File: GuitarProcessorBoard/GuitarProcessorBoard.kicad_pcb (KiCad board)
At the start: 4 copper layers, 86 x 65 mm, 136 parts, among them J301 SWD Header, J302 PWR, J303 TAP, J304 MODE, J305 BYP, J306 EXP, J307 ScopeGroundLoop, SW301 RST, SW302 BOOT, U201 TLV320AIC3204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

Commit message: enclosure SVG stuff
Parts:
- U303: value SSD1306_OLED_128x64 -> ~

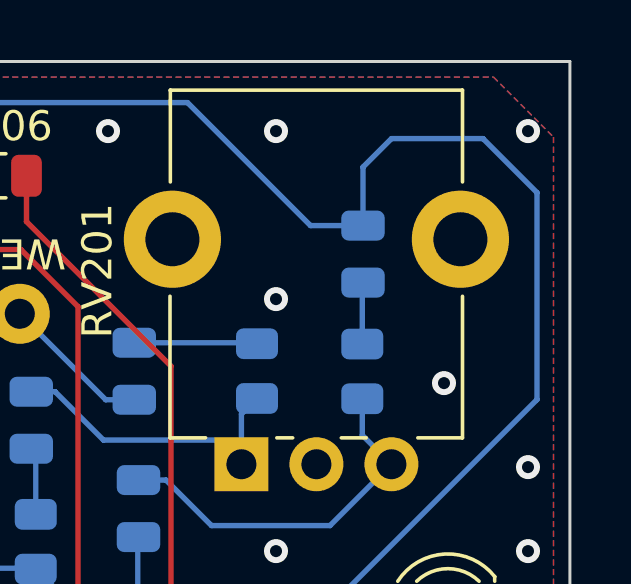
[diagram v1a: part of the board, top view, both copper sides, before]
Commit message: processing callback set up
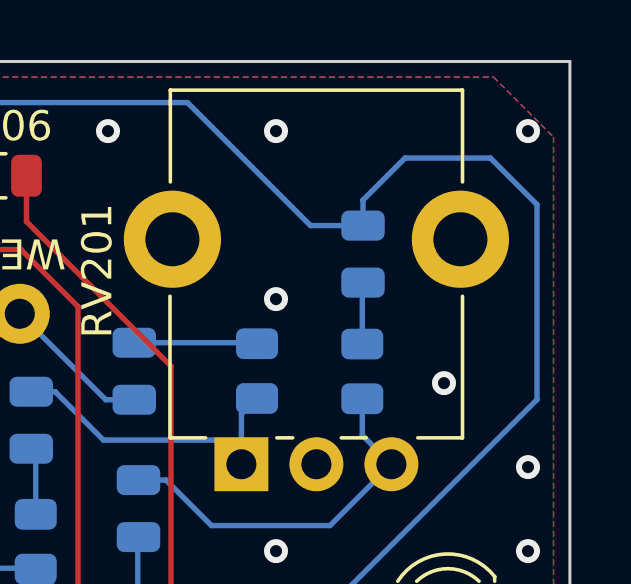
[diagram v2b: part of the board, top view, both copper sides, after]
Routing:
- net FX_IN: track 134.8 -> 133.4 mm
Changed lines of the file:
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@@
 	)
 	(footprint "Potentiometer_THT:Potentiometer_Alpha_RD901F-40-00D_Single_Vertical_CircularHoles"
+		(locked yes)
 		(layer "F.Cu")
 		(at -165.4 86.249999 90)
@@
 	)
 	(footprint "Potentiometer_THT:Potentiometer_Alpha_RD901F-40-00D_Single_Vertical_CircularHoles"
+		(locked yes)
 		(layer "F.Cu")
 		(at -103.903222 44.405189 90)
@@
 	)
 	(footprint "Potentiometer_THT:Potentiometer_Alpha_RD901F-40-00D_Single_Vertical_CircularHoles"
+		(locked yes)
 		(layer "F.Cu")
 		(at -140.348389 86.199999 90)
@@
 	)
 	(footprint "Potentiometer_THT:Potentiometer_Alpha_RD901F-40-00D_Single_Vertical_CircularHoles"
+		(locked yes)
 		(layer "F.Cu")
 		(at -115.296778 86.31981 90)
@@
 	)
 	(segment
-		(start -102.2 50.4)
-		(end -94.05 42.25)
+		(start -132.9 91.15)
+		(end -129.55 87.8)
 		(width 0.18)
 		(layer "B.Cu")
@@
 	)
 	(segment
-		(start -94.05 42.25)
-		(end -94.05 35.35)
+		(start -121.7 32.35)
+		(end -128.500001 39.150001)
 		(width 0.18)
 		(layer "B.Cu")
@@
 	)
 	(segment
-		(start -99.85 34.5)
-		(end -99.85 36.450001)
+		(start -98.45 34.2)
+		(end -99.85 35.6)
 		(width 0.18)
 		(layer "B.Cu")
@@
 	)
 	(segment
-		(start -132.9 91.15)
-		(end -129.55 87.8)
+		(start -102.2 50.4)
+		(end -94.05 42.25)
 		(width 0.18)
 		(layer "B.Cu")
@@
 	)
 	(segment
-		(start -121.7 32.35)
-		(end -128.500001 39.150001)
+		(start -132.9 92.8)
+		(end -132.9 91.15)
 		(width 0.18)
 		(layer "B.Cu")
@@
 	)
 	(segment
-		(start -94.05 35.35)
-		(end -95.85 33.55)
+		(start -101.599999 36.450001)
+		(end -105.7 32.35)
 		(width 0.18)
 		(layer "B.Cu")
@@
 	)
 	(segment
-		(start -95.85 33.55)
-		(end -98.9 33.55)
+		(start -94.05 42.25)
+		(end -94.05 35.75)
 		(width 0.18)
 		(layer "B.Cu")
@@
 	)
 	(segment
-		(start -132.9 92.8)
-		(end -132.9 91.15)
+		(start -99.85 35.6)
+		(end -99.85 36.450001)
 		(width 0.18)
 		(layer "B.Cu")
@@
 	)
 	(segment
-		(start -101.599999 36.450001)
-		(end -105.7 32.35)
+		(start -129.55 87.8)
+		(end -129.55 85.75)
 		(width 0.18)
 		(layer "B.Cu")
@@
 	)
 	(segment
-		(start -129.55 87.8)
-		(end -129.55 85.75)
+		(start -95.6 34.2)
+		(end -98.45 34.2)
 		(width 0.18)
 		(layer "B.Cu")
@@
 	)
 	(segment
-		(start -128.500001 39.150001)
-		(end -128.500001 45.7)
+		(start -94.05 35.75)
+		(end -95.6 34.2)
 		(width 0.18)
 		(layer "B.Cu")
@@
 	)
 	(segment
-		(start -98.9 33.55)
-		(end -99.85 34.5)
+		(start -128.500001 39.150001)
+		(end -128.500001 45.7)
 		(width 0.18)
 		(layer "B.Cu")

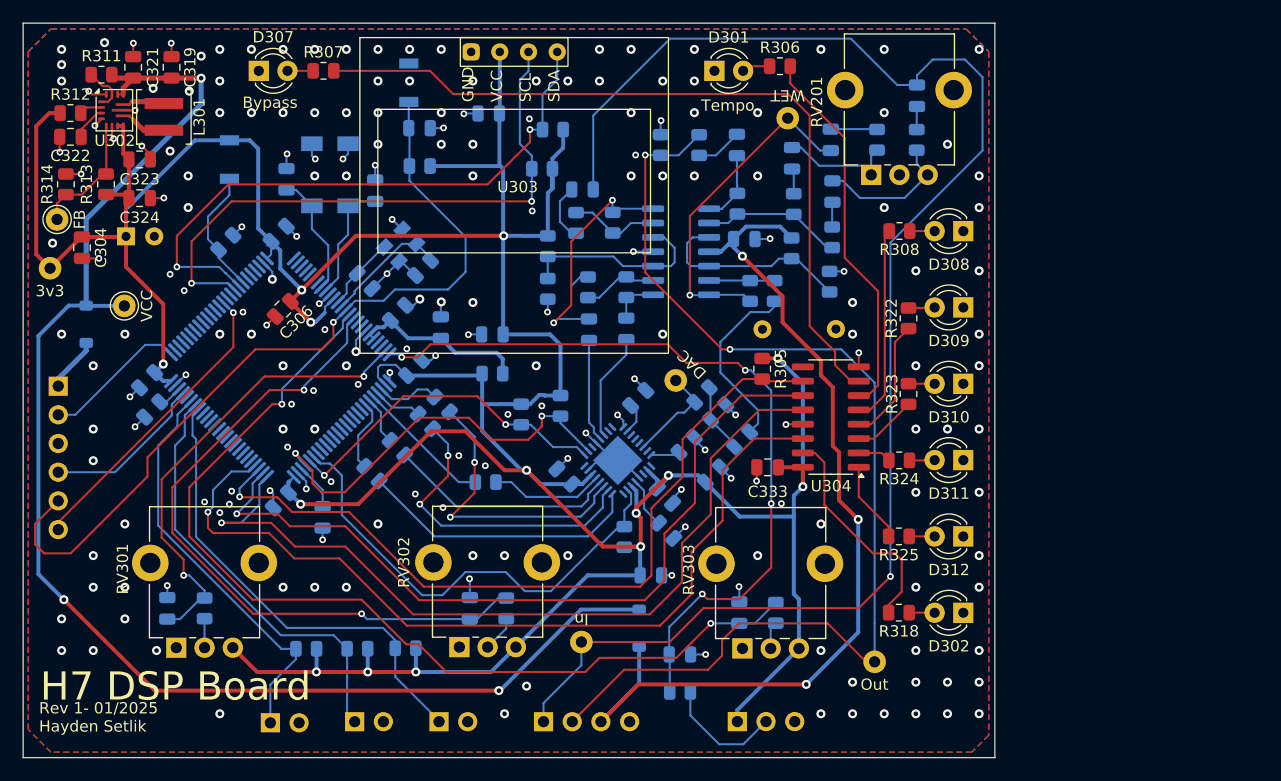
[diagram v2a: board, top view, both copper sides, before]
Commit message: differential output sim
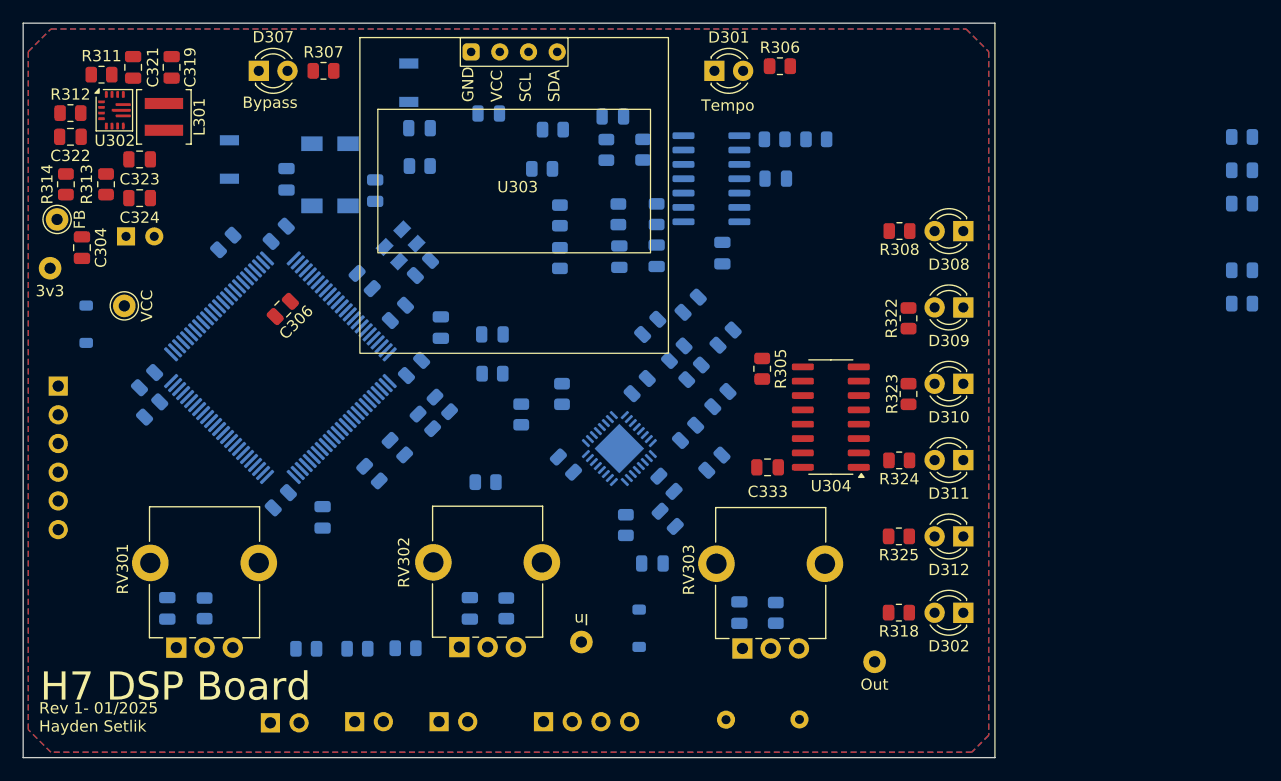
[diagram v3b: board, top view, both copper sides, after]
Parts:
- removed C217, C218: 100n, Capacitor_SMD:C_0805_2012Metric
- removed C219: 1u, Capacitor_SMD:C_0805_2012Metric
- removed C334: 10n, Capacitor_SMD:C_0805_2012Metric
- removed J306: EXP, Connector_PinHeader_2.54mm:PinHeader_1x03_P2.54mm_Vertical
- removed R217: 1M, Resistor_SMD:R_0805_2012Metric
- removed R218, R219: 10k, Resistor_SMD:R_0805_2012Metric
- removed R329: 470k, Resistor_SMD:R_0805_2012Metric
- removed RV201: 100kB, Potentiometer_THT:Potentiometer_Alpha_RD901F-40-00D_Single_Vertical_CircularHoles
- removed TP202: DAC, TestPoint:TestPoint_THTPad_D2.0mm_Drill1.0mm_VAL
- removed TP203: WET, TestPoint:TestPoint_THTPad_D2.0mm_Drill1.0mm_VAL
- added C208: 100n, Capacitor_SMD:C_0805_2012Metric, B.Cu at (-116.8, 58.8)
- C207: value 1u -> 4n7
- C214: value 1u -> 100n
- R204: value 470k -> 51k
- R205: value 470k -> 100k
- R213: value 47k -> 470k
- R214: value 47k -> 1k
- U303: value ~ -> SSD1306_OLED_128x64
- moved R212 44.8 mm to (-71.1, 44.0), turned to 180 degrees
- moved R211 43.6 mm to (-71.1, 41.0), turned to 180 degrees
- moved R215 40.1 mm to (-71.1, 52.9), turned to 180 degrees
- moved R216 36.7 mm to (-71.1, 55.8), turned to 180 degrees
- moved J307 34.7 mm to (-113.7, 92.6)
- moved R213 32.8 mm to (-71.1, 47.0), turned to 180 degrees
- moved C207 32.0 mm to (-117.2, 64.2), turned to 45 degrees
- moved R214 28.5 mm to (-119.6, 61.9), turned to 45 degrees
- moved C215 13.9 mm to (-117.1, 51.3), turned to -90 degrees
- moved C214 12.8 mm to (-119.9, 55.9)
- moved R210 12.7 mm to (-108.8, 41.3), turned to 0 degrees
- moved R209 9.76 mm to (-112.4, 41.3), turned to 0 degrees
- moved C212 9.66 mm to (-123.5, 57.9), turned to -135 degrees
- moved R205 7.00 mm to (-124.1, 42.2)
- moved C209 7.00 mm to (-126.8, 39.2)
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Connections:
- net /Audio/DAC_OUT renamed Net-(U201-OUT_L)
- C201 pad 1: +3.3V -> +3.3VA
- C202 pad 1: +3.3V -> +3.3VA
- C203 pad 1: +3.3V -> +3.3VA
- C207 pad 1: FX_IN -> Net-(C207-Pad1)
- C207 pad 2: Net-(C207-Pad2) -> GND
- C215 pad 2: Net-(C215-Pad2) -> FX_OUT
- R201 pad 1: +3.3V -> +3.3VA
- R202 pad 1: +3.3V -> +3.3VA
- R209 pad 2: /Audio/Bias2 -> Net-(U202A-+)
- R210 pad 1: /Audio/Bias2 -> Net-(U202A-+)
- R213 pad 1: Net-(C215-Pad2) -> /Audio/Bias2
- R213 pad 2: Net-(C217-Pad1) -> Net-(U202B--)
- R214 pad 1: Net-(C207-Pad2) -> Net-(U201-OUT_R)
- R214 pad 2: Net-(C218-Pad1) -> Net-(C207-Pad1)
- R215 pad 2: Net-(U202A--) -> Net-(U202B-+)
- R216 pad 1: Net-(C218-Pad2) -> Net-(U202B-+)
- R216 pad 2: Net-(U202A--) -> /Audio/Bias2
- U201 pad 23: unconnected-(U201-OUT_R-Pad23) -> Net-(U201-OUT_R)
- U201 pad 26: +3.3V -> +3.3VA
- U201 pad 30: +3.3V -> +3.3VA
- U201 pad 6: +3.3V -> +3.3VA
- U202 pad 1: Net-(C219-Pad1) -> /Audio/Bias2
- U202 pad 2: Net-(U202A--) -> /Audio/Bias2
- U202 pad 3: /Audio/Bias2 -> Net-(U202A-+)
- U202 pad 5: /Audio/Bias2 -> Net-(U202B-+)
- U301 pad 25: ADC_EXP -> unconnected-(U301-PA3-Pad25)
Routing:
- net +3.3V: track 363.5 -> 0.00 mm, vias 14 -> 0
- net FX_IN: track 133.4 -> 0.00 mm, vias 1 -> 0
- net VCC: track 124.9 -> 0.00 mm, vias 3 -> 0
- net FX_OUT: track 97.5 -> 0.00 mm, vias 2 -> 0
- net GND: track 85.7 -> 0.00 mm, vias 204 -> 0
- net ADC_C: track 85.4 -> 0.00 mm, vias 2 -> 0
- net +9V: track 82.1 -> 0.00 mm, vias 3 -> 0
- net LED_DATA: track 76.1 -> 0.00 mm, vias 1 -> 0
- net LED_LATCH: track 74.0 -> 0.00 mm, vias 1 -> 0
- net NRST: track 72.3 -> 0.00 mm, vias 1 -> 0
- net LED_SCK: track 70.9 -> 0.00 mm, vias 1 -> 0
- net /MCU/LED_BYPASS: track 69.5 -> 0.00 mm
- net LED_NRST: track 69.2 -> 0.00 mm, vias 1 -> 0
- net ADC_EXP: track 69.0 -> 0.00 mm, vias 4 -> 0
- net ADC_B: track 60.9 -> 0.00 mm, vias 2 -> 0
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
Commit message: routing start
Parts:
- removed D303: PMEG3030, Diode_SMD:D_SOD-123
- removed J303: TAP, Connector_PinHeader_2.54mm:PinHeader_1x02_P2.54mm_Vertical
- removed R213: 470k, Resistor_SMD:R_0805_2012Metric
- removed R326: 100k, Resistor_SMD:R_0805_2012Metric
- removed TP304: VCC, TestPoint:TestPoint_THTPad_D2.0mm_Drill1.0mm_VAL
- C215: value 1u -> 100n
- R211, R215: value 470k -> 100k
- R212, R216: value 470k -> 51k
- moved R212 41.1 mm to (-111.9, 48.5), turned to -90 degrees
- moved R211 38.4 mm to (-108.7, 48.6), turned to 90 degrees
- moved R216 36.3 mm to (-105.7, 45.0), turned to 90 degrees
- moved R215 34.9 mm to (-105.7, 48.6), turned to 90 degrees
- moved C303 30.8 mm to (-154.1, 77.6)
- moved J304 8.03 mm to (-157.6, 93.0)
- moved J305 6.37 mm to (-148.5, 93.2)
- moved R220 3.22 mm to (-134.8, 72.1)
- moved FB301 1.07 mm to (-137.4, 60.9), turned to 0 degrees
- moved C201 0.67 mm to (-121.5, 72.1)
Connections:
- J301 pad 1: Net-(D303-A) -> +3.3V
- U301 pad 70: TAP_BTN -> unconnected-(U301-PA11-Pad70)
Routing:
- net +3.3V: track 0.00 -> 140.8 mm, vias 0 -> 6
- net VCC: track 0.00 -> 137.3 mm, vias 0 -> 3
- net ADC_C: track 0.00 -> 106.9 mm, vias 0 -> 2
- net GND: track 0.00 -> 82.8 mm, vias 0 -> 51
- net LED_DATA: track 0.00 -> 80.3 mm, vias 0 -> 1
- net ADC_B: track 0.00 -> 79.5 mm, vias 0 -> 2
- net LED_LATCH: track 0.00 -> 75.8 mm, vias 0 -> 1
- net /MCU/LED_BYPASS: track 0.00 -> 69.0 mm
- net LED_NRST: track 0.00 -> 68.1 mm, vias 0 -> 1
- net LED_SCK: track 0.00 -> 67.2 mm, vias 0 -> 1
- net NRST: track 0.00 -> 60.2 mm, vias 0 -> 1
- net +3.3VA: track 0.00 -> 52.7 mm, vias 0 -> 3
- net BYP_BTN: track 0.00 -> 50.2 mm
- net ADC_A: track 0.00 -> 44.2 mm, vias 0 -> 2
- net MODE_BTN: track 0.00 -> 42.8 mm
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- removed copper zone on B.Cu, net GND
- removed copper zone on F.Cu, net GND
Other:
- board text added: "Rev 2- 07/2025 Hayden Setlik"
- board text removed: "3v3"
- board text removed: "EXP"
- board text removed: "Rev 1- 01/2025 Hayden Setlik"
- board text removed: "TAP"

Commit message: DRC passing
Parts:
- moved R303 0.95 mm to (-133.1, 44.8)
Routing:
- net +3.3V: track 140.8 -> 342.4 mm, vias 6 -> 12
- net +9V: track 17.0 -> 106.2 mm, vias 2 -> 3
- net FX_OUT: track 0.00 -> 77.8 mm, vias 0 -> 2
- net FX_IN: track 0.00 -> 76.6 mm, vias 0 -> 2
- net DISP_SDA: track 7.41 -> 46.1 mm, vias 0 -> 2
- net DISP_SCL: track 10.5 -> 44.2 mm, vias 0 -> 2
- net +3.3VA: track 52.7 -> 84.6 mm, vias 3 -> 4
- net /Audio/InputPos: track 0.00 -> 18.3 mm, vias 0 -> 2
- net Net-(U201-IN1_R): track 0.00 -> 16.4 mm
- net Net-(U201-IN1_L): track 0.00 -> 16.0 mm
- net /Audio/Bias1: track 4.76 -> 18.1 mm
- net GND: track 82.8 -> 90.5 mm, vias 51 -> 57
- net BYP_BTN: track 50.2 -> 43.5 mm
- net Net-(C209-Pad2): track 0.00 -> 6.19 mm
- net Net-(U202C--): track 2.50 -> 6.65 mm
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
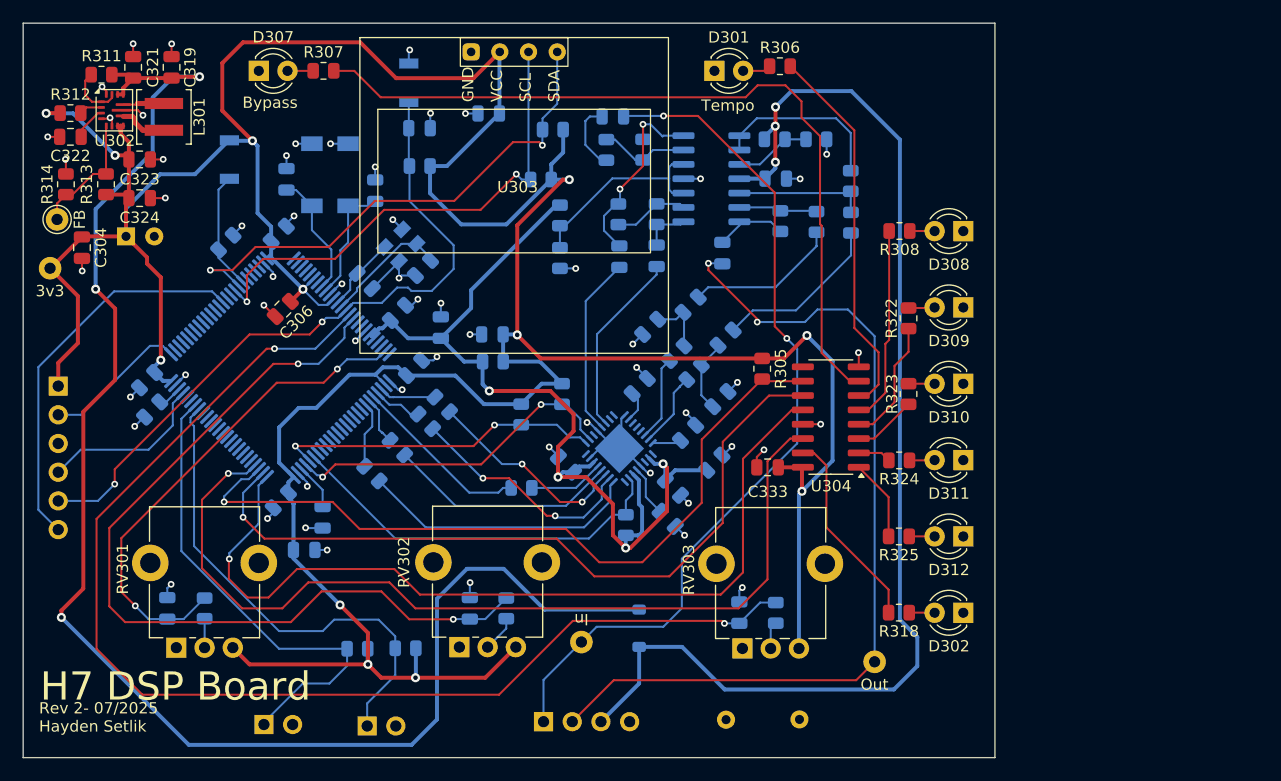
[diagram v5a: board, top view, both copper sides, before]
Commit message: more decoupling caps, return vias
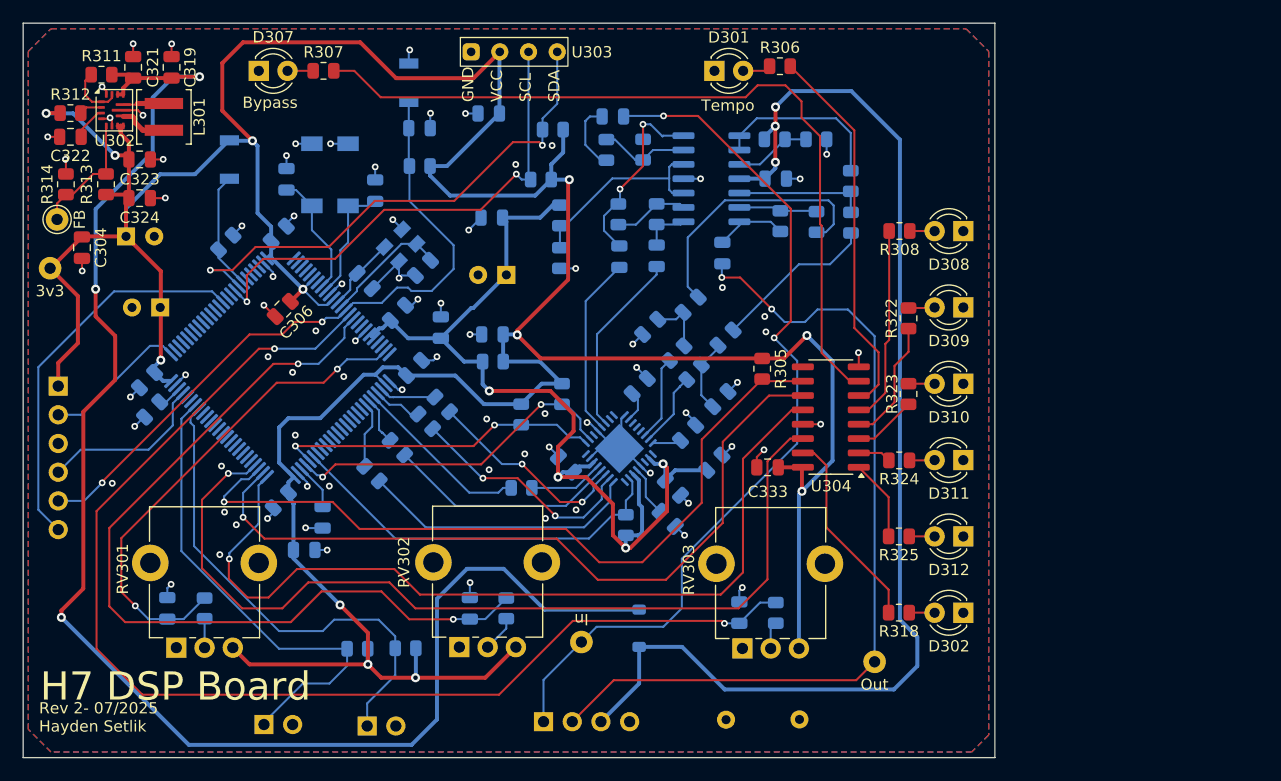
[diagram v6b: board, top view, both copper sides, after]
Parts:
- added C1: 330u, Capacitor_THT:CP_Radial_D5.0mm_P2.50mm, B.Cu at (-166.8, 56.1)
- added C2: 10u, Capacitor_SMD:C_0805_2012Metric, B.Cu at (-137.5, 48.2)
- added C3: 330u, Capacitor_THT:CP_Radial_D5.0mm_P2.50mm, B.Cu at (-136.2, 53.3)
- C209: value 1u -> 100n
- U303: footprint Display:SSD1306_OLED_128x64 -> Display:SSD1306_OLED_128x64_OffBoard
- moved U303 13.9 mm to (-135.5, 34.8)
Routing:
- net Net-(C214-Pad2): track 13.6 -> 23.6 mm
- net +3.3V: track 342.4 -> 339.0 mm
- net +3.3VA: track 84.6 -> 87.1 mm
- net FX_OUT: track 77.8 -> 75.6 mm
- net GND: track 90.5 -> 92.0 mm, vias 57 -> 80
- net FX_IN: track 76.6 -> 77.8 mm
- net NRST: track 60.9 -> 60.2 mm
- net Net-(C208-Pad2): track 15.2 -> 14.5 mm
- added copper zone on B.Cu, net GND
- added copper zone on F.Cu, net GND
